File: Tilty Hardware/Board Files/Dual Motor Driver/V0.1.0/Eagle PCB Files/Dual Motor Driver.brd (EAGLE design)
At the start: 50.8 x 50.8 mm, 25 parts, among them U1 ATMEGA32U4TQFP, U2 L298_BRIDGE_DRIVER

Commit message: Lots of work on dual motor driver
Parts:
- removed C2: 0.1uF, resistor:C0603
- removed JP10: (no value), SparkFun-Connectors:1X04-1MM-RA
- removed JP11, JP9: M11PTH, SparkFun-Connectors:1X11
- added C1, C7: 1uF, resistor:C0603
- added C3, C5, C6: 0.1uF, resistor:C0603
- added F1: PTCSMD, SparkFun-PowerIC:PTC-1206
- added J1: AVR_SPI_PRG_6PTH, SparkFun-Connectors:2X3
- added R1, R2: 10K, resistor:R0603
- added RN1: (no value), resistor-dil:0603-ARV
- added SJ1: SOLDERJUMPERNC, SparkFun-Passives:SJ_2S
- added U3: PCA9306, My Parts:SOIC-8
- added U4: TLV71333PDBVR, SparkFun-PowerIC:SOT23-5
- added U5: VOLTAGE-REGULATOR, My Parts:SOT89
- moved C4 52.3 mm to (17.8, 28.7)
- moved JP6 27.4 mm to (47.5, 9.40)
- moved JP5 8.40 mm to (3.30, 9.14)
- moved Z1 6.43 mm to (22.9, 43.4), turned to 90 degrees
- moved D2 1.30 mm to (37.5, 16.9)
- moved D3 1.30 mm to (13.8, 16.9)
- moved D6 1.30 mm to (15.9, 16.9)
- moved D7 1.30 mm to (35.4, 16.9)
- moved U2 1.30 mm to (25.7, 15.2)
- moved D1 1.30 mm to (37.5, 10.9)
- moved D4 1.30 mm to (13.8, 10.9)
- moved D5 1.30 mm to (15.9, 10.9)
- moved D8 1.30 mm to (35.4, 10.9)
- moved U1 1.11 mm to (25.4, 33.3), turned to 90 degrees
- moved Z2 0.51 mm to (28.4, 43.4), turned to 90 degrees
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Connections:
- removed net VUSB: JP7.VBUS, U1.7
- new net +3V3: C3.1, U3.P$2, U4.5
- new net L-SCL: JP4.7, U3.P$3
- new net L-SDA: JP4.8, U3.P$4
- new net MISO: J1.1, U1.11
- new net MOSI: J1.4, U1.10
- new net N$1: RN1.5, U1.4
- new net N$2: RN1.8, U1.3
- new net N$3: R2.1, U3.P$8
- new net N$4: F1.2, JP7.VBUS
- new net N$5: JP2.2, SJ1.1
- new net RESET: J1.5, R1.1, U1.13
- new net SCK: J1.3, U1.9
- net +24V: now also C7.1, JP8.4, SJ1.2, U5.P$3
- net +5V: now also C1.1, C5.1, C6.1, F1.1, J1.2, R1.2, R2.2, U1.6, U1.7, U3.P$7, U4.1, U4.3, U5.P$1; no longer C2.1
- net GND: now also C3.2, C5.2, C6.2, C7.2, J1.6, JP8.3, U2.10, U3.P$1, U4.2, U5.P$2, U5.P$4; no longer C2.2, U2.19, U2.2, U2.20
- net H-SCL: now also U3.P$6; no longer JP4.7
- net H-SDA: now also U3.P$5; no longer JP4.8
- net M1A: now also JP8.6
- net M1B: now also JP8.5
- net M2A: now also JP5.P$5, JP8.2
- net M2B: now also JP5.P$6, JP8.1
- net UGND: now also C1.2
- net USB_D+: now also RN1.4; no longer U1.4
- net USB_D-: now also RN1.1; no longer U1.3

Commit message: Updated dual motor driver and Tilty Duo/Quad PCBs, added a copuple experimental arduino programs
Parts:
- added C2, C8: 22pF, resistor:C0603
- added Q1: 16MHz, crystal:CTS406
- moved J1 28.2 mm to (62.7, 21.3), turned to 180 degrees
- moved R1 5.59 mm to (39.4, 30.2), turned to 90 degrees
- moved R2 0.25 mm to (45.0, 32.0)
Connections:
- new net N$6: C8.2, Q1.3, U1.17
- new net N$7: C2.2, Q1.1, U1.16
- net GND: now also C2.1, C8.1
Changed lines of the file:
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@@
 </element>
 <element name="JP8" library="SparkFun-Connectors" package="SCREWTERMINAL-3.5MM-6" value="" x="16.764" y="3.556"/>
-<element name="J1" library="SparkFun-Connectors" package="2X3" value="AVR_SPI_PRG_6PTH" x="35.052" y="26.67" smashed="yes" rot="R270"/>
-<element name="R1" library="resistor" package="R0603" value="10K" x="33.782" y="29.972" smashed="yes"/>
+<element name="J1" library="SparkFun-Connectors" package="2X3" value="AVR_SPI_PRG_6PTH" x="62.738" y="21.336" smashed="yes" rot="R180"/>
+<element name="R1" library="resistor" package="R0603" value="10K" x="39.37" y="30.226" smashed="yes" rot="R90"/>
 <element name="RN1" library="resistor-dil" package="0603-ARV" value="" x="25.654" y="43.688" smashed="yes" rot="R180">
 <attribute name="OC_NEWARK" value="unknown" x="25.654" y="43.688" size="1.778" layer="27" rot="R180" display="off"/>
@@
 <attribute name="PART#" value="PCA9306D,118" x="41.148" y="35.56" size="1.778" layer="27" rot="R270" display="off"/>
 </element>
-<element name="R2" library="resistor" package="R0603" value="10K" x="44.704" y="32.004" smashed="yes" rot="R270"/>
+<element name="R2" library="resistor" package="R0603" value="10K" x="44.958" y="32.004" smashed="yes" rot="R270"/>
 <element name="U4" library="SparkFun-PowerIC" package="SOT23-5" value="TLV71333PDBVR" x="33.782" y="41.656" smashed="yes" rot="R180">
 <attribute name="PROD_ID" value="VREG-11306" x="33.782" y="41.656" size="1.778" layer="27" rot="R180" display="off"/>
@@
 </element>
 <element name="SJ1" library="SparkFun-Passives" package="SJ_2S" value="SOLDERJUMPERNC" x="9.398" y="7.112"/>
+<element name="Q1" library="crystal" package="CTS406" value="16MHz" x="34.29" y="26.289" smashed="yes">
+<attribute name="OC_NEWARK" value="unknown" x="34.29" y="26.289" size="1.778" layer="27" display="off"/>
+<attribute name="MPN" value="" x="34.29" y="26.289" size="1.778" layer="27" display="off"/>
+<attribute name="MF" value="" x="34.29" y="26.289" size="1.778" layer="27" display="off"/>
+<attribute name="OC_FARNELL" value="unknown" x="34.29" y="26.289" size="1.778" layer="27" display="off"/>
+<attribute name="PART#" value="406C35D16M00000" x="34.29" y="26.289" size="1.778" layer="27" display="off"/>
+</element>
+<element name="C2" library="resistor" package="C0603" value="22pF" x="33.02" y="23.368" smashed="yes" rot="R180"/>
+<element name="C8" library="resistor" package="C0603" value="22pF" x="35.56" y="29.21" smashed="yes"/>
 </elements>
 <signals>
@@
 <contactref element="U2" pad="1"/>
 <contactref element="U2" pad="10"/>
+<contactref element="C2" pad="1"/>
+<contactref element="C8" pad="1"/>
 <wire x1="43.053" y1="38.21" x2="43.268" y2="40.132" width="0" layer="19" extent="1-1"/>
 <wire x1="33.782" y1="42.9561" x2="43.268" y2="40.132" width="0" layer="19" extent="1-1"/>
@@
 <wire x1="13.843" y1="9.222" x2="13.843" y2="18.591" width="0" layer="19" extent="1-1"/>
 <wire x1="32.385" y1="20.955" x2="31.2" y2="31.674" width="0" layer="19" extent="1-1"/>
-<wire x1="37.592" y1="21.59" x2="32.385" y2="20.955" width="0" layer="19" extent="1-1"/>
-<wire x1="37.465" y1="18.591" x2="37.592" y2="21.59" width="0" layer="19" extent="1-1"/>
+<wire x1="37.465" y1="18.591" x2="32.385" y2="20.955" width="0" layer="19" extent="1-1"/>
 <wire x1="37.465" y1="9.222" x2="37.465" y2="18.591" width="0" layer="19" extent="1-1"/>
 <wire x1="32.385" y1="9.525" x2="37.465" y2="9.222" width="0" layer="19" extent="1-1"/>
 <wire x1="23.764" y1="3.556" x2="32.385" y2="9.525" width="0" layer="19" extent="1-1"/>
+<wire x1="33.87" y1="23.368" x2="13.843" y2="9.222" width="0" layer="19" extent="1-1"/>
+<wire x1="34.71" y1="29.21" x2="33.87" y2="23.368" width="0" layer="19" extent="1-1"/>
+<wire x1="57.658" y1="18.796" x2="37.465" y2="18.591" width="0" layer="19" extent="1-1"/>
 </signal>
 <signal name="M1A">
@@
 <contactref element="C6" pad="1"/>
 <contactref element="U5" pad="P$1"/>
-<wire x1="34.732" y1="42.9561" x2="34.632" y2="44.704" width="0" layer="19" extent="1-1"/>
-<wire x1="32.832" y1="42.9561" x2="34.732" y2="42.9561" width="0" layer="19" extent="1-1"/>
-<wire x1="30.988" y1="42.034" x2="32.832" y2="42.9561" width="0" layer="19" extent="1-1"/>
-<wire x1="28.6" y1="39.074" x2="30.988" y2="42.034" width="0" layer="19" extent="1-1"/>
-<wire x1="31.2" y1="30.874" x2="28.6" y2="39.074" width="0" layer="19" extent="1-1"/>
-<wire x1="34.632" y1="29.972" x2="31.2" y2="30.874" width="0" layer="19" extent="1-1"/>
-<wire x1="37.592" y1="26.67" x2="34.632" y2="29.972" width="0" layer="19" extent="1-1"/>
+<wire x1="44.958" y1="31.154" x2="62.738" y2="18.796" width="0" layer="19" extent="1-1"/>
+<wire x1="41.783" y1="32.91" x2="44.958" y2="31.154" width="0" layer="19" extent="1-1"/>
+<wire x1="39.37" y1="31.076" x2="41.783" y2="32.91" width="0" layer="19" extent="1-1"/>
+<wire x1="31.2" y1="30.874" x2="39.37" y2="31.076" width="0" layer="19" extent="1-1"/>
 <wire x1="26.2" y1="27.474" x2="31.2" y2="30.874" width="0" layer="19" extent="1-1"/>
 <wire x1="25.4" y1="27.474" x2="26.2" y2="27.474" width="0" layer="19" extent="1-1"/>
@@
 <wire x1="13.374" y1="21.59" x2="13.237" y2="23.113" width="0" layer="19" extent="1-1"/>
 <wire x1="18.923" y1="19.685" x2="13.374" y2="21.59" width="0" layer="19" extent="1-1"/>
-<wire x1="41.783" y1="32.91" x2="37.592" y2="26.67" width="0" layer="19" extent="1-1"/>
-<wire x1="44.704" y1="31.154" x2="41.783" y2="32.91" width="0" layer="19" extent="1-1"/>
 <wire x1="19.6" y1="37.274" x2="19.6" y2="29.274" width="0" layer="19" extent="1-1"/>
+<wire x1="28.6" y1="39.074" x2="31.2" y2="30.874" width="0" layer="19" extent="1-1"/>
+<wire x1="30.988" y1="42.034" x2="28.6" y2="39.074" width="0" layer="19" extent="1-1"/>
+<wire x1="32.832" y1="42.9561" x2="30.988" y2="42.034" width="0" layer="19" extent="1-1"/>
+<wire x1="34.732" y1="42.9561" x2="32.832" y2="42.9561" width="0" layer="19" extent="1-1"/>
+<wire x1="34.632" y1="44.704" x2="34.732" y2="42.9561" width="0" layer="19" extent="1-1"/>
 </signal>
 <signal name="USB_D-">
@@
 <contactref element="R1" pad="1"/>
 <contactref element="U1" pad="13"/>
-<wire x1="31.2" y1="30.074" x2="32.932" y2="29.972" width="0" layer="19" extent="1-1"/>
-<wire x1="35.052" y1="21.59" x2="32.932" y2="29.972" width="0" layer="19" extent="1-1"/>
+<wire x1="39.37" y1="29.376" x2="57.658" y2="21.336" width="0" layer="19" extent="1-1"/>
+<wire x1="31.2" y1="30.074" x2="39.37" y2="29.376" width="0" layer="19" extent="1-1"/>
 </signal>
 <signal name="SCK">
 <contactref element="U1" pad="9"/>
 <contactref element="J1" pad="3"/>
-<wire x1="27.8" y1="27.474" x2="35.052" y2="24.13" width="0" layer="19" extent="1-1"/>
+<wire x1="27.8" y1="27.474" x2="60.198" y2="21.336" width="0" layer="19" extent="1-1"/>
 </signal>
 <signal name="MOSI">
 <contactref element="U1" pad="10"/>
 <contactref element="J1" pad="4"/>
-<wire x1="28.6" y1="27.474" x2="37.592" y2="24.13" width="0" layer="19" extent="1-1"/>
+<wire x1="28.6" y1="27.474" x2="60.198" y2="18.796" width="0" layer="19" extent="1-1"/>
 </signal>
 <signal name="MISO">
 <contactref element="U1" pad="11"/>
 <contactref element="J1" pad="1"/>
-<wire x1="29.4" y1="27.474" x2="35.052" y2="26.67" width="0" layer="19" extent="1-1"/>
+<wire x1="29.4" y1="27.474" x2="62.738" y2="21.336" width="0" layer="19" extent="1-1"/>
 </signal>
 <signal name="N$1">
@@
 <contactref element="U3" pad="P$8"/>
 <contactref element="R2" pad="1"/>
-<wire x1="43.053" y1="32.91" x2="44.704" y2="32.854" width="0" layer="19" extent="1-1"/>
+<wire x1="43.053" y1="32.91" x2="44.958" y2="32.854" width="0" layer="19" extent="1-1"/>
 </signal>
 <signal name="+3V3">
@@
 <wire x1="8.9861" y1="7.112" x2="8.89" y2="13.843" width="0" layer="19" extent="1-1"/>
 </signal>
+<signal name="N$6">
+<contactref element="Q1" pad="3"/>
+<contactref element="C8" pad="2"/>
+<contactref element="U1" pad="17"/>
+<wire x1="31.2" y1="33.274" x2="36.49" y2="27.489" width="0" layer="19" extent="1-1"/>
+<wire x1="36.41" y1="29.21" x2="36.49" y2="27.489" width="0" layer="19" extent="1-1"/>
+</signal>
+<signal name="N$7">
+<contactref element="Q1" pad="1"/>
+<contactref element="C2" pad="2"/>
+<contactref element="U1" pad="16"/>
+<wire x1="32.09" y1="25.089" x2="31.2" y2="32.474" width="0" layer="19" extent="1-1"/>
+<wire x1="32.17" y1="23.368" x2="32.09" y2="25.089" width="0" layer="19" extent="1-1"/>
+</signal>
 </signals>

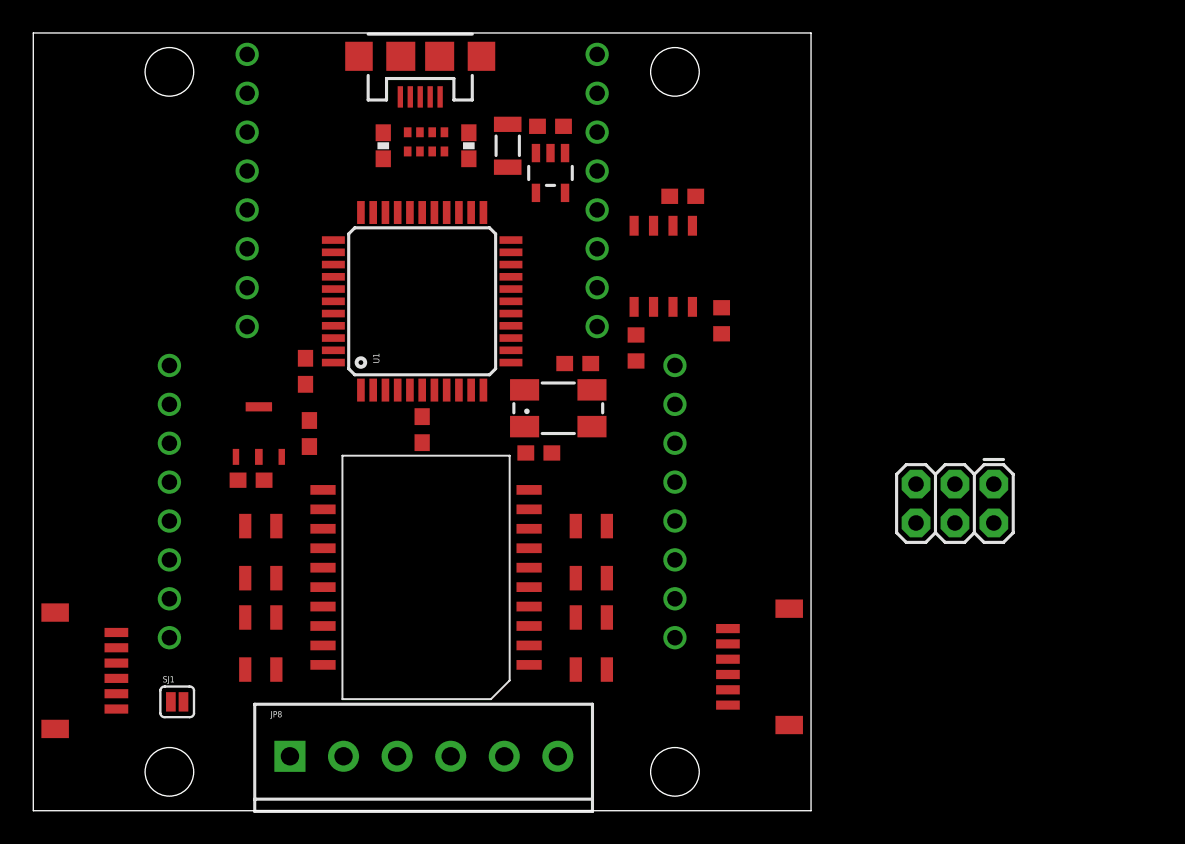
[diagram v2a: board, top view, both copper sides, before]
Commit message: Dual motor driver add-on design
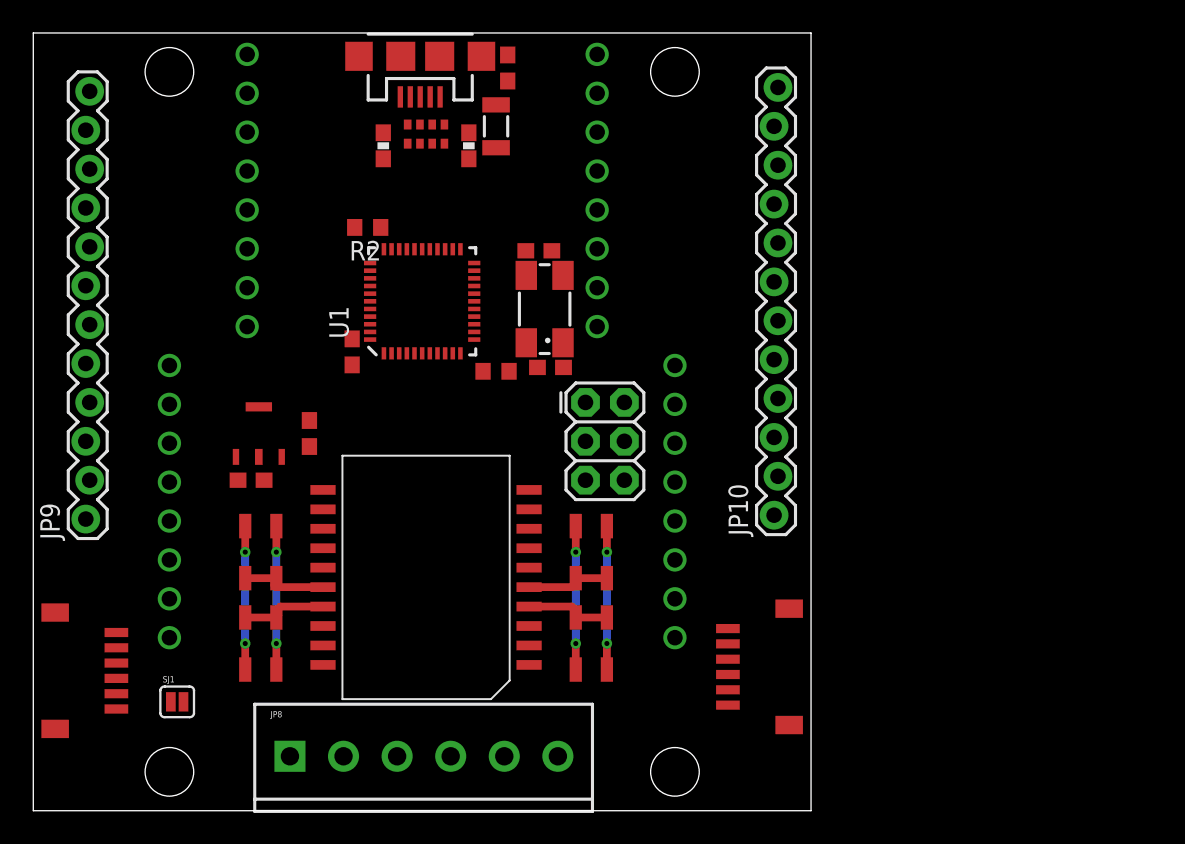
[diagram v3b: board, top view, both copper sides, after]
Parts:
- removed C3, C5: 0.1uF, resistor:C0603
- removed U3: PCA9306, My Parts:SOIC-8
- removed U4: TLV71333PDBVR, SparkFun-PowerIC:SOT23-5
- added JP10, JP9: M12LOCK, SparkFun-Connectors:1X12_LOCK
- U1: value ATMEGA32U4TQFP -> ATMEGA32U4QFN2; device SparkFun-DigitalIC:SPARKFUN-DIGITALIC_TQFP44 -> SparkFun-DigitalIC:SPARKFUN-DIGITALIC_QFN-44-NOPAD
- moved J1 27.2 mm to (36.1, 26.7), turned to 270 degrees
- moved C1 24.3 mm to (31.0, 48.5), turned to 90 degrees
- moved R2 23.9 mm to (21.8, 38.1), turned to 180 degrees
- moved R1 9.27 mm to (30.2, 28.7), turned to 0 degrees
- moved C8 7.79 mm to (33.0, 36.6), turned to 180 degrees
- moved Q1 6.54 mm to (33.4, 32.8), turned to 90 degrees
- moved C2 5.64 mm to (33.8, 29.0), turned to 0 degrees
- moved C4 3.30 mm to (20.8, 30.0)
- moved F1 1.48 mm to (30.2, 44.7)
- moved RN1 0.51 mm to (25.7, 44.2)
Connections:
- removed net +3V3: C3.1, U3.P$2, U4.5
- removed net H-SCL: U1.18, U3.P$6
- removed net H-SDA: U1.19, U3.P$5
- removed net L-SCL: JP4.7, U3.P$3
- removed net L-SDA: JP4.8, U3.P$4
- removed net N$3: R2.1, U3.P$8
- new net AI0: U1.36
- new net AI1: U1.37
- new net AI2: U1.38
- new net AI3: U1.39
- new net AI4: U1.40
- new net AI5: U1.41
- new net DIO0/RX: U1.20
- new net DIO1/TX: U1.21
- new net DIO10: U1.30
- new net DIO11: U1.12
- new net DIO12: U1.26
- new net DIO13: U1.32
- new net DIO4: U1.25
- new net DIO5: U1.31
- new net DIO6: U1.27
- new net DIO7: U1.1
- new net DIO8: U1.28
- new net DIO9: U1.29
- new net SCL: JP3.7, U1.18
- new net SDA: JP3.8, U1.19
- new net SS/RXLED: U1.8
- new net TXLED: U1.22
- new net |HWB: R2.1, U1.33
- net +5V: no longer C5.1, U3.P$7, U4.1, U4.3
- net GND: no longer C3.2, C5.2, U3.P$1, U4.2
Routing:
- net GND: track 0.00 -> 18.7 mm, vias 0 -> 4
- net +24V: track 0.00 -> 18.7 mm, vias 0 -> 4
- net M2A: track 0.00 -> 5.77 mm
- net M1A: track 0.00 -> 5.64 mm
- net M2B: track 0.00 -> 5.64 mm
- net M1B: track 0.00 -> 5.52 mm
